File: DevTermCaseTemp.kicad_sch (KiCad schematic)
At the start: 1 part, among them J1 miniPCIe

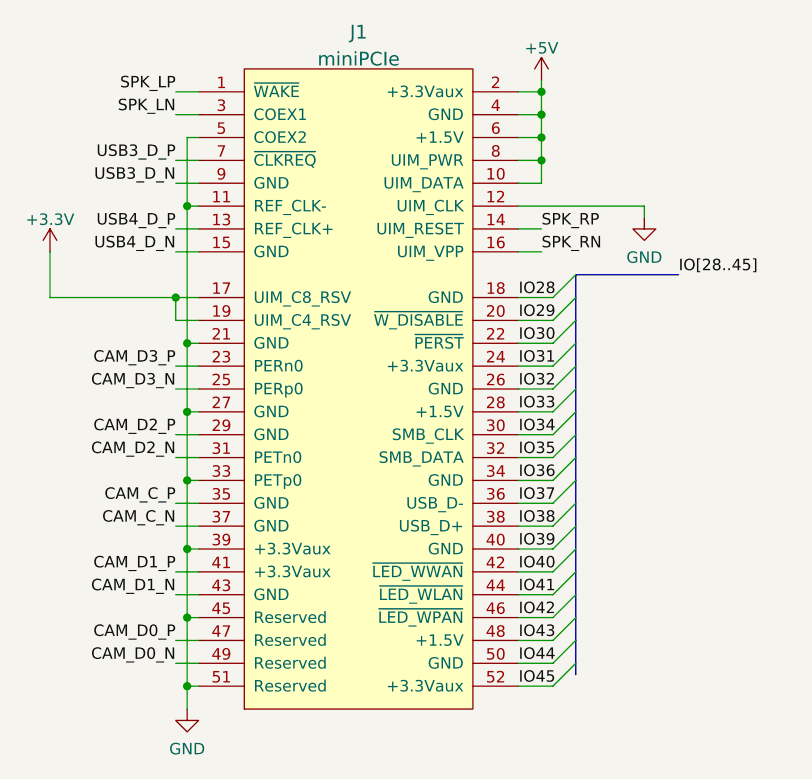
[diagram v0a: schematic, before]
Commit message: Update the symbol of mPCIE port
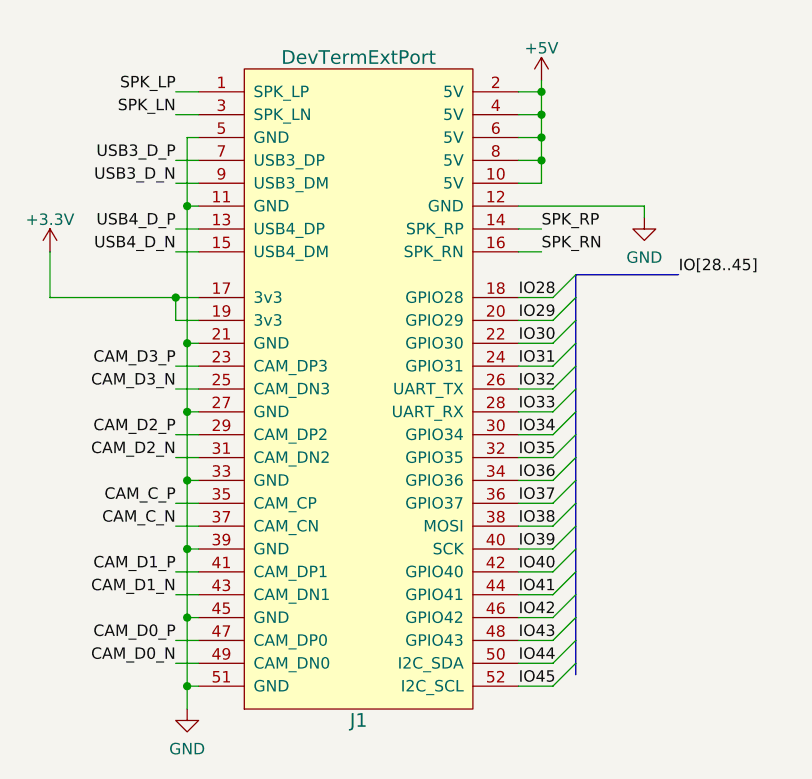
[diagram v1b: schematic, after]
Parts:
- J1: value miniPCIe -> DevTermExtPort; symbol mpcie:miniPCIe -> mpcie:DevTermExtPort
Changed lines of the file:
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@@
   (symbol (lib_id "power:+3.3V") (at 21.59 40.64 0) (unit 1)
     (in_bom yes) (on_board yes) (fields_autoplaced)
-    (property "Reference" "#PWR?" (id 0) (at 21.59 44.45 0)
+    (property "Reference" "#PWR01" (id 0) (at 21.59 44.45 0)
       (effects (font (size 1.27 1.27)) hide)
     )
@@
   (symbol (lib_id "power:GND") (at 87.63 36.83 0) (unit 1)
     (in_bom yes) (on_board yes) (fields_autoplaced)
-    (property "Reference" "#PWR?" (id 0) (at 87.63 43.18 0)
+    (property "Reference" "#PWR04" (id 0) (at 87.63 43.18 0)
       (effects (font (size 1.27 1.27)) hide)
     )
@@
   (symbol (lib_id "power:+5V") (at 76.2 21.59 0) (unit 1)
     (in_bom yes) (on_board yes) (fields_autoplaced)
-    (property "Reference" "#PWR0101" (id 0) (at 76.2 25.4 0)
+    (property "Reference" "#PWR03" (id 0) (at 76.2 25.4 0)
       (effects (font (size 1.27 1.27)) hide)
     )
@@
     (pin "1")
   )
-  (symbol (lib_id "mpcie:miniPCIe") (at 55.88 54.61 0) (unit 1)
+  (symbol (lib_id "mpcie:DevTermExtPort") (at 55.88 54.61 0) (unit 1)
     (in_bom yes) (on_board yes) (fields_autoplaced)
-    (property "Reference" "J1" (id 0) (at 55.88 16.2359 0)
+    (property "Reference" "J1" (id 0) (at 55.88 92.71 0)
       (effects (font (size 1.524 1.524)))
     )
-    (property "Value" "miniPCIe" (id 1) (at 55.88 19.2293 0)
+    (property "Value" "DevTermExtPort" (id 1) (at 55.88 19.05 0)
       (effects (font (size 1.524 1.524)))
     )
@@
   (symbol (lib_id "power:GND") (at 36.83 91.44 0) (unit 1)
     (in_bom yes) (on_board yes) (fields_autoplaced)
-    (property "Reference" "#PWR?" (id 0) (at 36.83 97.79 0)
+    (property "Reference" "#PWR02" (id 0) (at 36.83 97.79 0)
       (effects (font (size 1.27 1.27)) hide)
     )
@@
   )
   (symbol_instances
+    (path "/36775b63-f971-490c-9534-dba42ba8b7a5"
+      (reference "#PWR01") (unit 1) (value "+3.3V") (footprint "")
+    )
+    (path "/ce81fc0e-e190-4d3a-8e6b-96dcaf3d51a1"
+      (reference "#PWR02") (unit 1) (value "GND") (footprint "")
+    )
     (path "/b93c28e7-59ef-487c-8478-662ac5cdfc6f"
-      (reference "#PWR0101") (unit 1) (value "+5V") (footprint "")
-    )
-    (path "/36775b63-f971-490c-9534-dba42ba8b7a5"
-      (reference "#PWR?") (unit 1) (value "+3.3V") (footprint "")
+      (reference "#PWR03") (unit 1) (value "+5V") (footprint "")
     )
     (path "/3ddfe0dd-397d-4aa7-ad10-0f6b2d19d573"
-      (reference "#PWR?") (unit 1) (value "GND") (footprint "")
-    )
-    (path "/ce81fc0e-e190-4d3a-8e6b-96dcaf3d51a1"
-      (reference "#PWR?") (unit 1) (value "GND") (footprint "")
+      (reference "#PWR04") (unit 1) (value "GND") (footprint "")
     )
     (path "/c8840939-c132-4052-b289-a80b63045b95"
-      (reference "J1") (unit 1) (value "miniPCIe") (footprint "mpcie:mini-PCIe")
+      (reference "J1") (unit 1) (value "DevTermExtPort") (footprint "mpcie:mini-PCIe")
     )
   )
